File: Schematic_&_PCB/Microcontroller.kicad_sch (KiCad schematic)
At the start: 26 parts, among them J1 GCT USB4105, SW21 ~{RESET}, SW22 ~{USB_BOOT}, U1 RP2040, U2 W25Q32JVZP, U3 NCP1117ST33T3G, U4 USBLC6-2SC6, Y1 12MHz

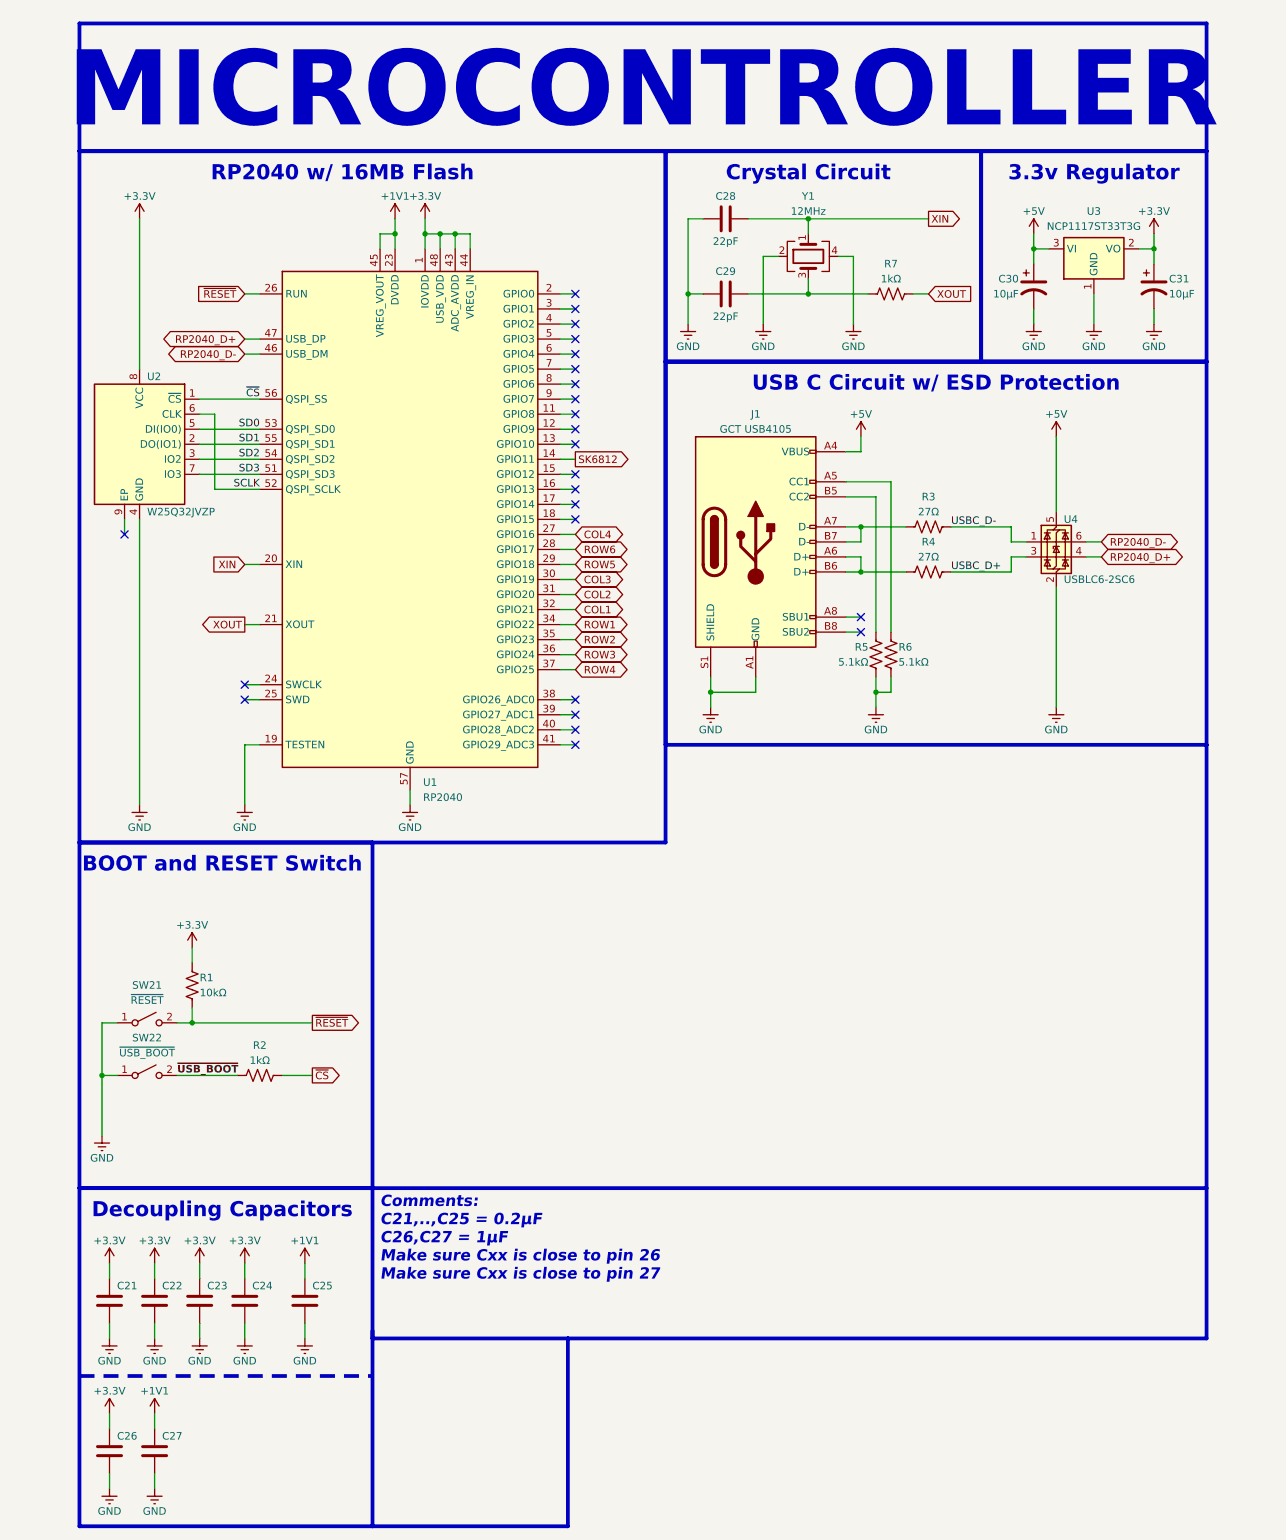
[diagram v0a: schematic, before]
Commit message: changed the mcu
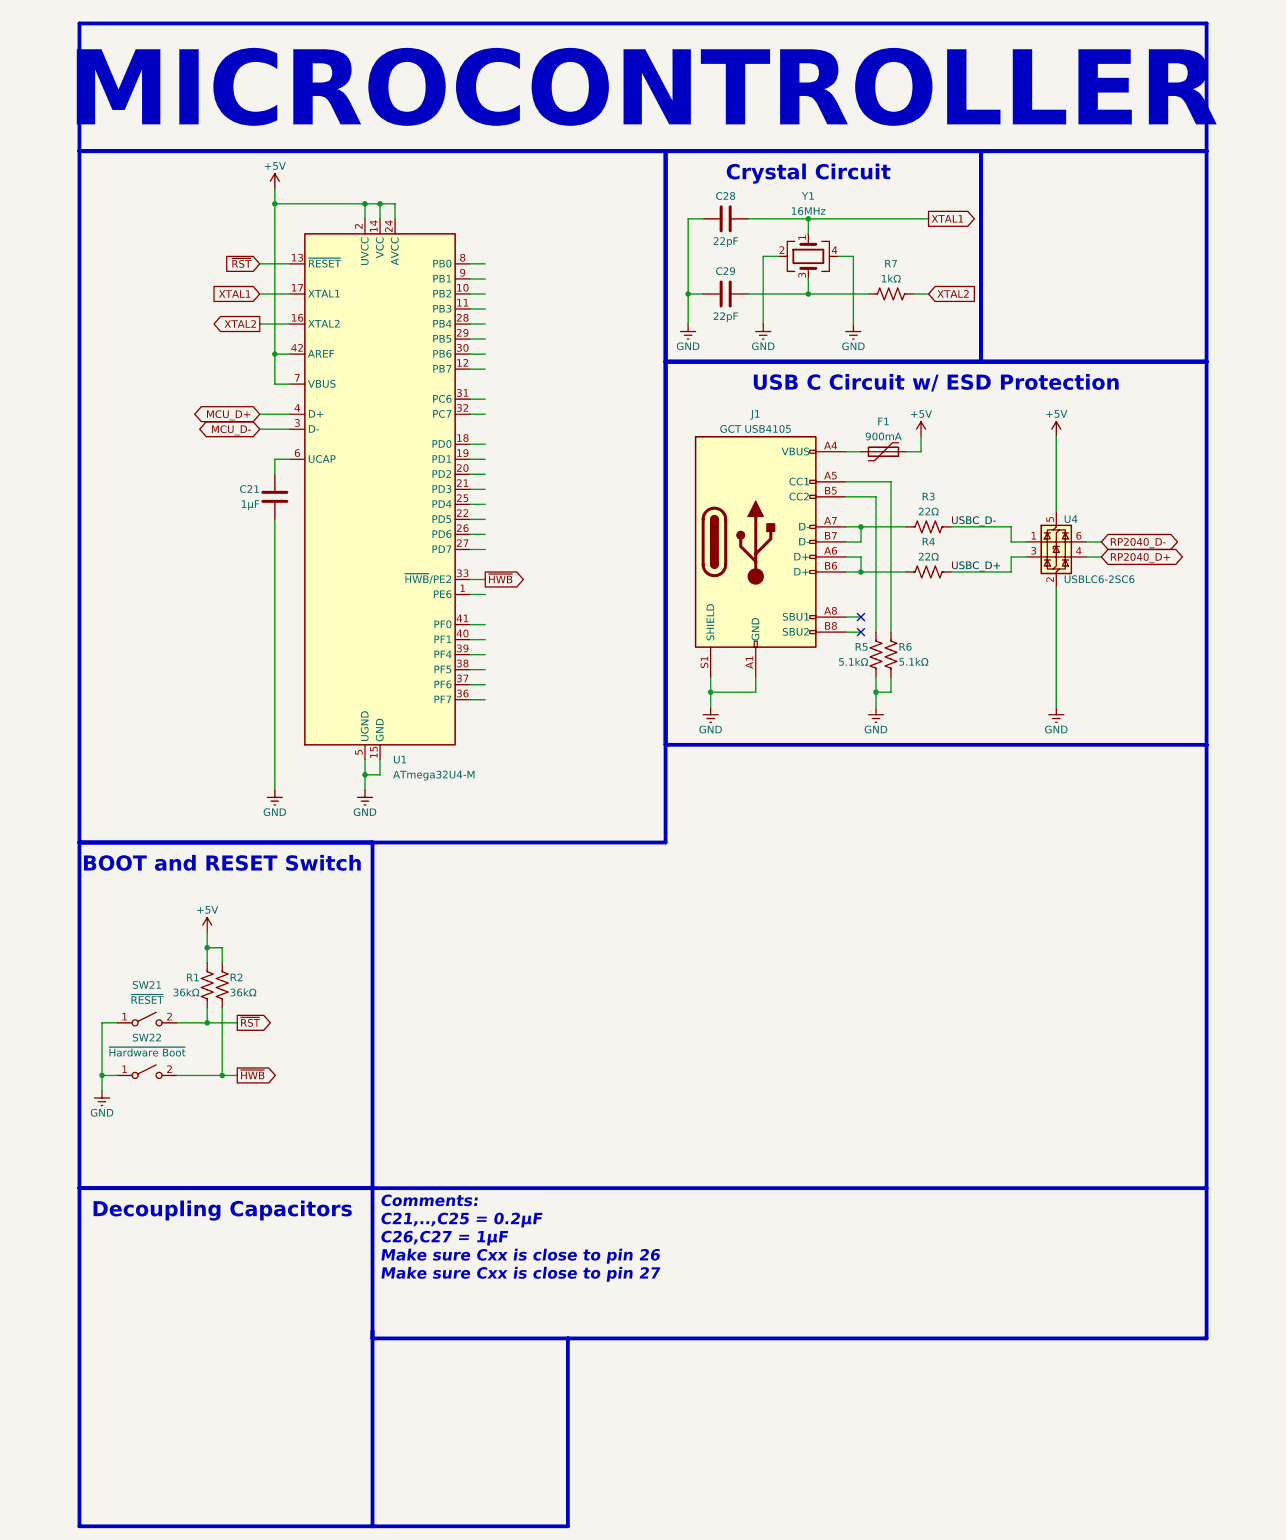
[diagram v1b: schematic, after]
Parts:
- removed C22, C23, C24, C25: 0.2μF, Capacitor_SMD:C_0603_1608Metric, symbol Device:C
- removed C26, C27: 1μF, Capacitor_SMD:C_0603_1608Metric, symbol Device:C
- removed C30, C31: 10μF, Capacitor_Tantalum_SMD:CP_EIA-3216-10_Kemet-I, symbol Device:C_Polarized_US
- removed U1: RP2040, Package_DFN_QFN:QFN-56-1EP_7x7mm_P0.4mm_EP3.2x3.2mm, symbol MCU_RaspberryPi:RP2040
- removed U2: W25Q32JVZP, Package_SON:WSON-8-1EP_6x5mm_P1.27mm_EP3.4x4.3mm, symbol Memory_Flash:W25Q32JVZP
- removed U3: NCP1117ST33T3G, Package_TO_SOT_SMD:SOT-223-3_TabPin2, symbol Regulator_Linear:NCP1117-3.3_SOT223
- added F1: 900mA, Fuse:Fuse_1206_3216Metric, symbol Device:Polyfuse
- added U1: ATmega32U4-M, Package_DFN_QFN:QFN-44-1EP_7x7mm_P0.5mm_EP5.2x5.2mm, symbol MCU_Microchip_ATmega:ATmega32U4-M
- C21: value 0.2μF -> 1µF; footprint Capacitor_SMD:C_0603_1608Metric -> Capacitor_SMD:C_0402_1005Metric
- R1: value 10kΩ -> 36kΩ
- R2: value 1kΩ -> 36kΩ
- R3, R4: value 27Ω -> 22Ω
- SW22: value ~{USB_BOOT} -> ~{Hardware Boot}
- Y1: value 12MHz -> 16MHz
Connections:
- net +5V: now also R1.1, R2.1, F1.2, U1.14 (VCC), U1.2 (UVCC), U1.24 (AVCC), U1.34 (VCC), U1.42 (AREF), U1.44 (AVCC), U1.7 (VBUS); no longer J1.A4 (VBUS), J1.A9 (VBUS), J1.B4 (VBUS), J1.B9 (VBUS)
- net GND: now also C21.1, U1.15 (GND), U1.23 (GND), U1.35 (GND), U1.43 (GND), U1.45 (GND), U1.5 (UGND); no longer C21.2
- removed net +3.3V: C21.1, R1.1
- net XIN renamed XTAL1
- net XTAL1: now also U1.17 (XTAL1)
- net XOUT renamed XTAL2
- net XTAL2: now also U1.16 (XTAL2)
- net ~{CS} renamed ~{HWB}
- net ~{HWB}: now also SW22.2 (B), U1.33 (~{HWB}/PE2)
- net ~{RESET} renamed ~{RST}
- net ~{RST}: now also U1.13 (~{RESET})
- removed net ~{USB_BOOT}: R2.1, SW22.2 (B)
- new net: C21.2, U1.6 (UCAP)
- new net: F1.1, J1.A4 (VBUS), J1.A9 (VBUS), J1.B4 (VBUS), J1.B9 (VBUS)
- new net MCU_D+: U1.4 (D+)
- new net MCU_D-: U1.3 (D-)
- no-connect marks 24 -> 2
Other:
- note removed: "3.3v Regulator"
- note removed: "RP2040 w/ 16MB Flash"
- moved on the sheet: R1
